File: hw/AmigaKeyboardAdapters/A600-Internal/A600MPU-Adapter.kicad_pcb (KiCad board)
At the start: 2 copper layers, 33 x 29.2 mm, 9 parts, among them P1 CONN_02X03, P2 CONN_01X03, U1 6571R4_PLCC44_MPUKEY_REV

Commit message: From KiCAD 4 to KiCAD 5
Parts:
- C1, C3: footprint Capacitors_SMD:c_elec_3x5.3 -> Capacitor_Tantalum_SMD:CP_EIA-3216-12_Kemet-S_Pad1.58x1.35mm_HandSolder
- C2, C4: footprint Capacitors_SMD:C_0603_HandSoldering -> Capacitor_SMD:C_1206_3216Metric_Pad1.33x1.80mm_HandSolder
- D1: value Led_Small -> RED; footprint SMD_Packages:SMD-1206_Pol -> LED_SMD:LED_1206_3216Metric_Pad1.42x1.75mm_HandSolder
- P1: footprint Pin_Headers:Pin_Header_Straight_2x03 -> Connector_IDC:IDC-Header_2x03_P2.54mm_Vertical
- P2: footprint Pin_Headers:Pin_Header_Straight_1x03 -> Connector_PinHeader_2.54mm:PinHeader_1x03_P2.54mm_Vertical
- R1: value 330 -> 330R; footprint Resistors_SMD:R_0603_HandSoldering -> Resistor_SMD:R_1206_3216Metric_Pad1.30x1.75mm_HandSolder
- U1: footprint Sockets:PLCC44 -> RetroBitLab:PLCC-44_THT-Socket_3D
- moved U1 6.11 mm to (168.6, 103.2), turned to 90 degrees
- moved R1 3.82 mm to (163.0, 118.1)
- moved D1 3.21 mm to (171.5, 118.2)
- moved C4 1.00 mm to (153.4, 118.1), turned to 0 degrees
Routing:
- net ~RST: track 27.3 -> 13.6 mm
- net ~TRESET: track 29.9 -> 18.4 mm, vias 0 -> 1
- net VCC: track 68.6 -> 78.0 mm
- net KBD_DATA: track 10.4 -> 17.7 mm
- net KBD_RESET: track 20.3 -> 25.2 mm, vias 0 -> 1
- net GND: track 55.9 -> 54.4 mm, vias 0 -> 1
- net KBD_CLOCK: track 12.8 -> 11.7 mm
- net Net-(D1-Pad1): track 6.39 -> 5.52 mm
- added copper zone on F.Cu, net GND
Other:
- rule pad_to_mask_clearance: 0.2 -> 0
- board text added: "designed by R.G.2018/2022"
- board text removed: "designed by R.G.2018"

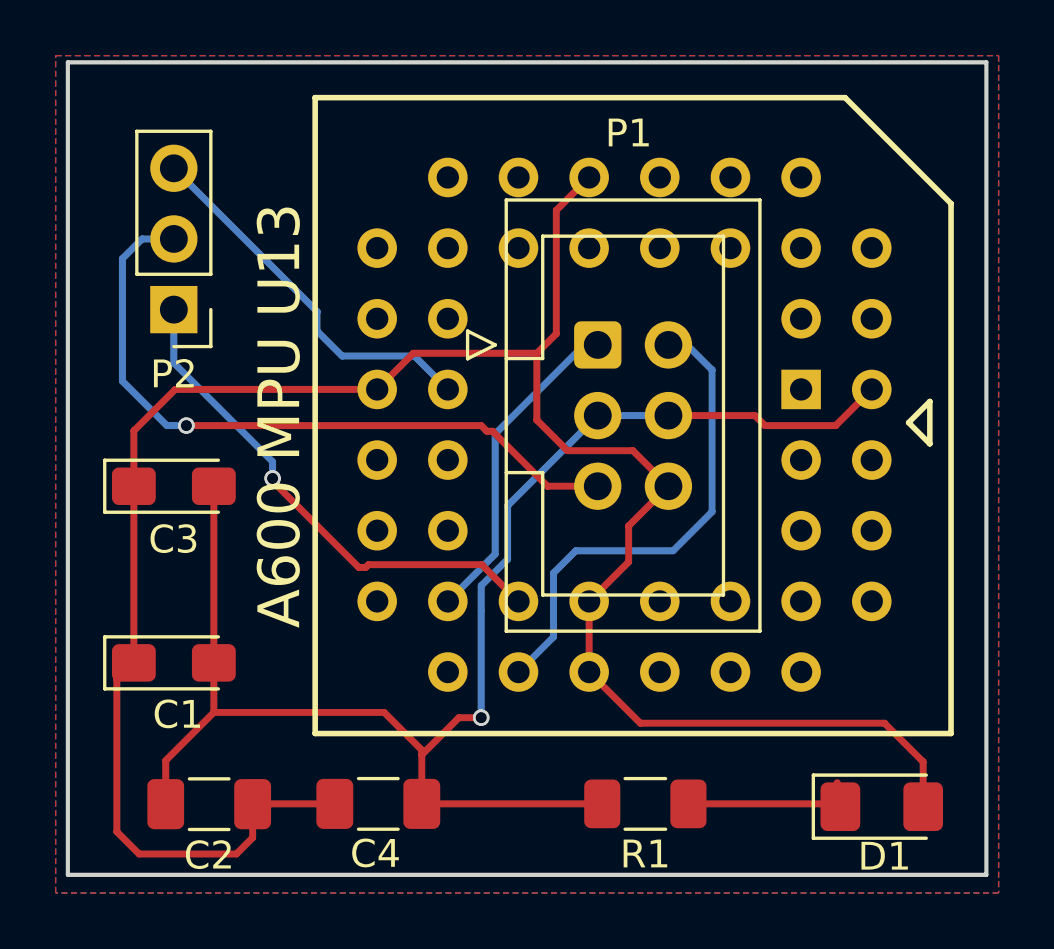
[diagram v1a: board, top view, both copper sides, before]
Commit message: Updated PWR_FLAGs and other symbols
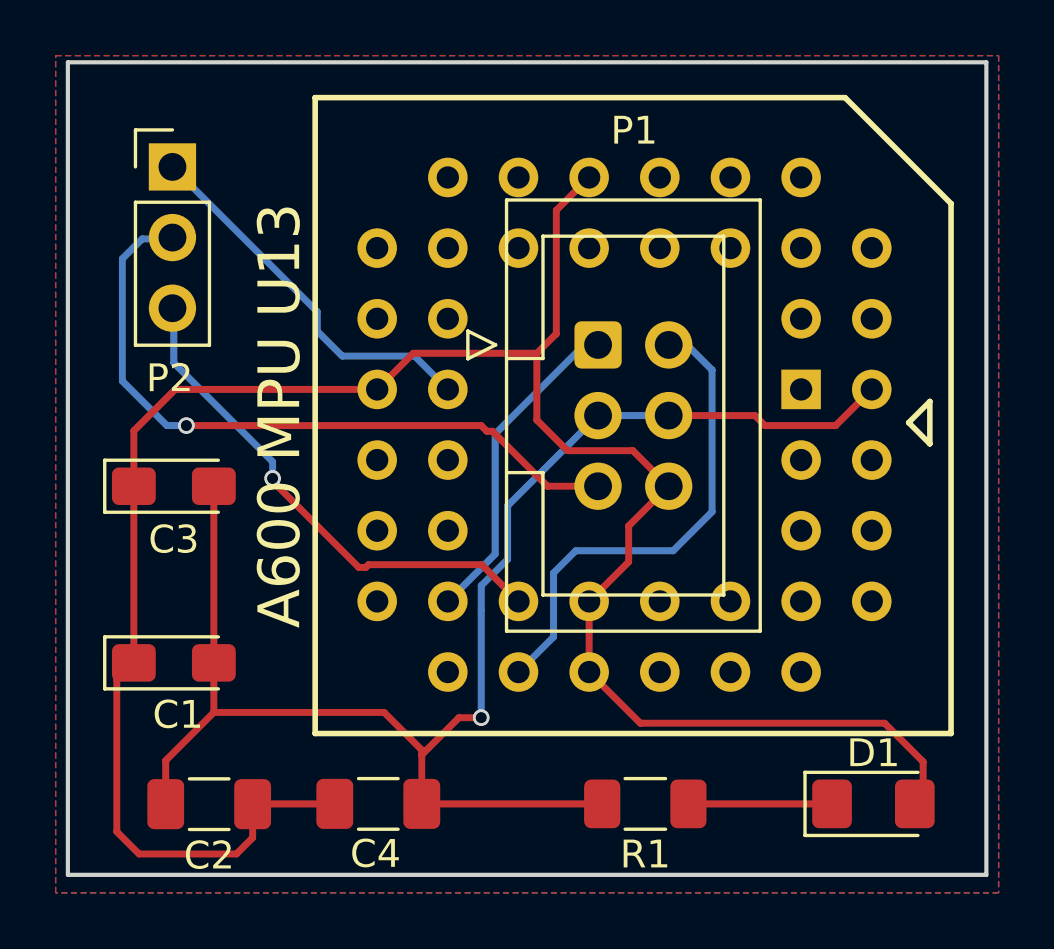
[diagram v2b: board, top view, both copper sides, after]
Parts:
- P1: value CONN_02X03 -> Conn_02x03_Odd_Even
- P2: value CONN_01X03 -> Conn_01x03_Male
- moved P2 5.13 mm to (146.0, 95.2), turned to 0 degrees
- moved D1 0.32 mm to (171.2, 118.1)
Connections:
- P2 pad 1: ~TRESET -> ~RST
- P2 pad 3: ~RST -> ~TRESET
